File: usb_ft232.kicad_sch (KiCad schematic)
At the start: 16 parts, among them J4 USB_C_Receptacle_USB2.0, U3 FT232RL, U6 USBLC6-2SC6

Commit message: finish update extra updates
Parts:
- added R39, R40: 10k, Resistor_SMD:R_1206_3216Metric, symbol Device:R
- renumbered U3 to U4
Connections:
- net GND: now also R39.1, R40.1
- net cc1: now reaches J4.A5 (CC1)
- net cc1: now also R39.2
- net cc2: now reaches J4.B5 (CC2)
- net cc2: now also R40.2
- no-connect marks 16 -> 14
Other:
- note added: "USB position and shield"
- moved on the sheet: C19, R14

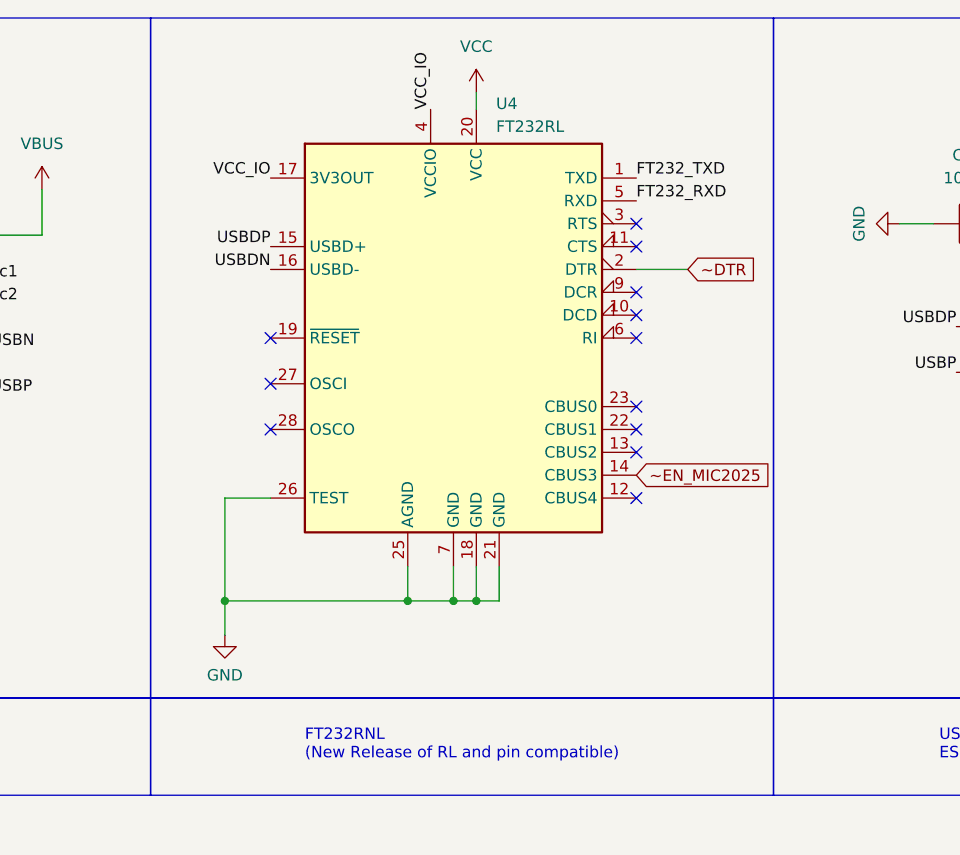
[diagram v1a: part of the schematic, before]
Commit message: clock fix for FT232RL and update cleaner routes
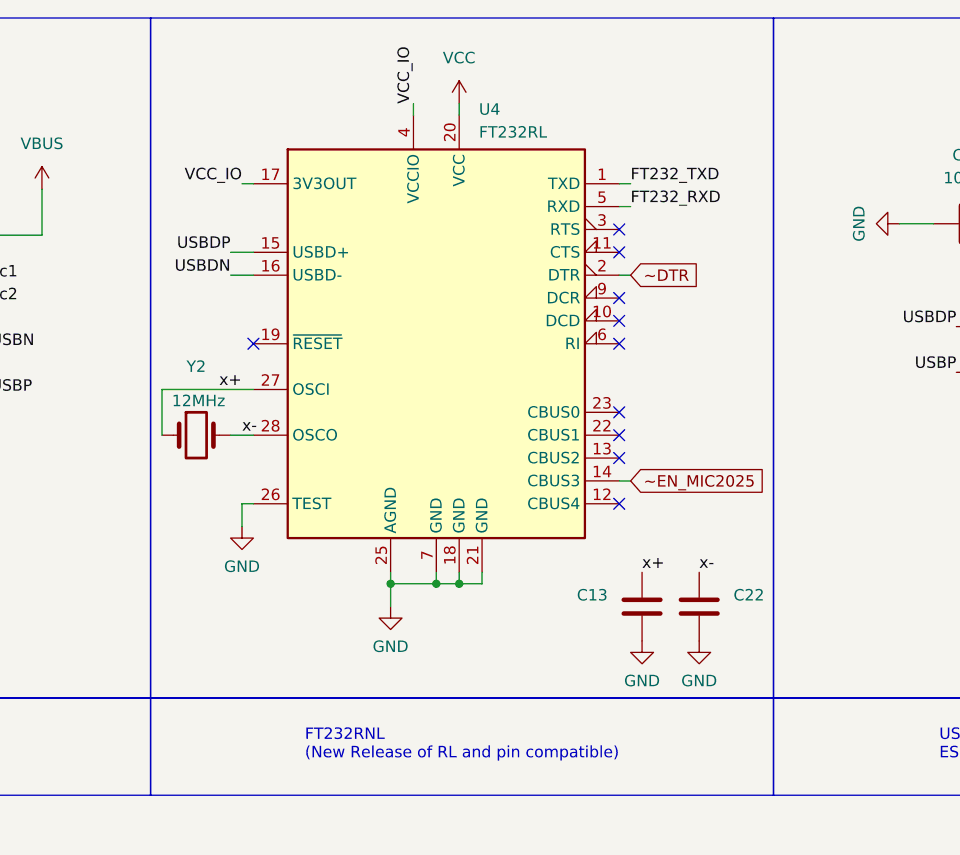
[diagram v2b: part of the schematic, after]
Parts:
- added C13, C22: ~, Capacitor_SMD:C_0402_1005Metric, symbol Device:C
- added Y2: 12MHz, Crystal:Crystal_C38-LF_D3.0mm_L8.0mm_Vertical, symbol Device:Crystal
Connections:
- net GND: now also C13.2, C22.2
- net x+: now reaches U4.27 (OSCI)
- net x+: now also C13.1, Y2.1
- net x-: now reaches U4.28 (OSCO)
- net x-: now also C22.1, Y2.2
- no-connect marks 14 -> 12
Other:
- moved on the sheet: U4
